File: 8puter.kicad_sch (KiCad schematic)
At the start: 6 parts, among them J1 PWR-DC

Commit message: Serial interface
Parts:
- removed CPU1: W65C816SxP, Package_DIP:DIP-40_W25.4mm_LongPads, symbol 65xx:W65C816SxP
- removed R6: 1K, Resistor_SMD:R_0603_1608Metric, symbol Device:R
- added C2: 1uF, symbol Device:C_Small
- added CPU1: W65C02SxP, Package_DIP:DIP-40_W25.4mm_LongPads, symbol 65xx:W65C02SxP
- added GLUE_FPGA1: (no value), Package_DFN_QFN:QFN-32-1EP_5x5mm_P0.5mm_EP3.1x3.1mm, symbol Custom:﻿MachXO2-256-QFN32
- added JTAG1: (no value), Connector_PinHeader_1.00mm:PinHeader_1x05_P1.00mm_Vertical, symbol Connector_Generic:Conn_01x05
- added R1: 1K, symbol Device:R
- added R3: 4.7K, symbol Device:R
- C3: value 10uF -> 10uF 16V
- C4: footprint Capacitor_SMD:C_1206_3216Metric_Pad1.33x1.80mm_HandSolder -> (none)
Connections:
- net +3V3: now also GLUE_FPGA1.15 (VCCIO2), GLUE_FPGA1.18 (VCC), GLUE_FPGA1.19 (VCCIO1), GLUE_FPGA1.2 (VCC), GLUE_FPGA1.24 (VCCIO0), GLUE_FPGA1.31 (VCCIO0), GLUE_FPGA1.6 (VCCIO3), GLUE_FPGA1.7 (VCCIO2), R1.2
- net +5V: now also C2.1, CPU1.38 (~{SO}), CPU1.8 (VDD)
- net ADDR0: now also CPU1.9 (A0)
- net ADDR1: now also CPU1.10 (A1)
- net ADDR10: now also CPU1.19 (A10)
- net ADDR11: now also CPU1.20 (A11)
- net ADDR12: now also CPU1.22 (A12), GLUE_FPGA1.17 (PB9B/SI)
- net ADDR13: now also CPU1.23 (A13), GLUE_FPGA1.16 (PB9A/SN)
- net ADDR14: now also CPU1.24 (A14), GLUE_FPGA1.14 (PB4D)
- net ADDR15: now also CPU1.25 (A15), GLUE_FPGA1.13 (PB4C)
- net ADDR2: now also CPU1.11 (A2)
- net ADDR3: now also CPU1.12 (A3)
- net ADDR4: now also CPU1.13 (A4)
- net ADDR5: now also CPU1.14 (A5)
- net ADDR6: now also CPU1.15 (A6)
- net ADDR7: now also CPU1.16 (A7)
- net ADDR8: now also CPU1.17 (A8)
- net ADDR9: now also CPU1.18 (A9)
- net BE: now also CPU1.36 (BE), GLUE_FPGA1.10 (PB2D/SPISO)
- net CLOCK: now also CPU1.37 (ϕ0), GLUE_FPGA1.9 (PB2C/SCLK)
- net CPU_R~{W}: now also CPU1.34 (R/~{W}), GLUE_FPGA1.12 (PB4B)
- net GND: now also C2.2, CPU1.21 (VSS), GLUE_FPGA1.22 (GND), GLUE_FPGA1.3 (GND), GLUE_FPGA1.33 (GND), JTAG1.4 (Pin_4), R3.2
- net RDY: now also CPU1.2 (RDY), GLUE_FPGA1.11 (PB4A)
- net ~{IRQ}: now also CPU1.4 (~{IRQ})
- net ~{NMI}: now also CPU1.6 (~{NMI})
- new net: GLUE_FPGA1.26 (PT9A/JTAGENB), R1.1
- new net CPU_W~{R}: GLUE_FPGA1.21 (PR5A)
- new net DATA0: CPU1.33 (D0)
- new net DATA1: CPU1.32 (D1)
- new net DATA2: CPU1.31 (D2)
- new net DATA3: CPU1.30 (D3)
- new net DATA4: CPU1.29 (D4)
- new net DATA5: CPU1.28 (D5)
- new net DATA6: CPU1.27 (D6)
- new net DATA7: CPU1.26 (D7)
- new net TCK: GLUE_FPGA1.30 (PT7A/TCK), JTAG1.2 (Pin_2), R3.1
- new net TDI: GLUE_FPGA1.32 (PT6D/TDI), JTAG1.3 (Pin_3)
- new net TDO: GLUE_FPGA1.1 (PT6C/TDO), JTAG1.5 (Pin_5)
- new net TMS: GLUE_FPGA1.29 (PT7B/TMS), JTAG1.1 (Pin_1)
- new net ~{PRP_CS}: GLUE_FPGA1.25 (PT9B/PROGRAMN)
- new net ~{RAM_CS}: GLUE_FPGA1.28 (PT8C/SCL)
- new net ~{RESET}: CPU1.40 (~{RES})
- new net ~{ROM_CS}: GLUE_FPGA1.27 (PT8D/SDA)
- new net ~{SERIAL_CS}: GLUE_FPGA1.20 (PR5B)
- new net ~{VID_CS}: GLUE_FPGA1.23 (PT9D/DONE)
- no-connect marks 1 -> 8
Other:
- removed sheet Bus Control
- added sheet Serial Controller (sch/serial.kicad_sch)
- sheet Memory Unit ports: added A[0..15], ~{ROM_CS}, ~{SRAM_CS}; removed A[0..23], VA, ~{PRP_CS[0..5]}, ~{VID_CS}
- sheet Peripheral Handler ports: added A[0..15], BUS_R~{W}, ~{PRP_CS}, ~{RESET}; removed BUS_EN, ~{PRP_CS[0..5]}
- sheet Power ports: added ~{RST}; removed RST
- note added: "DEBUG"
- note added: "MEMORY MAP ~{ }"
- note added: "RAM: 0x0000 - 0x7FFF PRP: 0x8000 - 0x8FFF SER: 0x9000 - 0x9FFF VID: 0xA000 - 0xAFFF ROM: 0xB000 - 0xFFFF"
- note added: "This map will be programmed into the FPGA"
- note removed: "Contains ROM, RAM and decode logic."
- note removed: "Debug"
- note removed: "MEMORY"
- company: (none) -> zrthxn
- title: (none) -> 8puter
- moved on the sheet: C3, C4, CRYSTAL0, J1

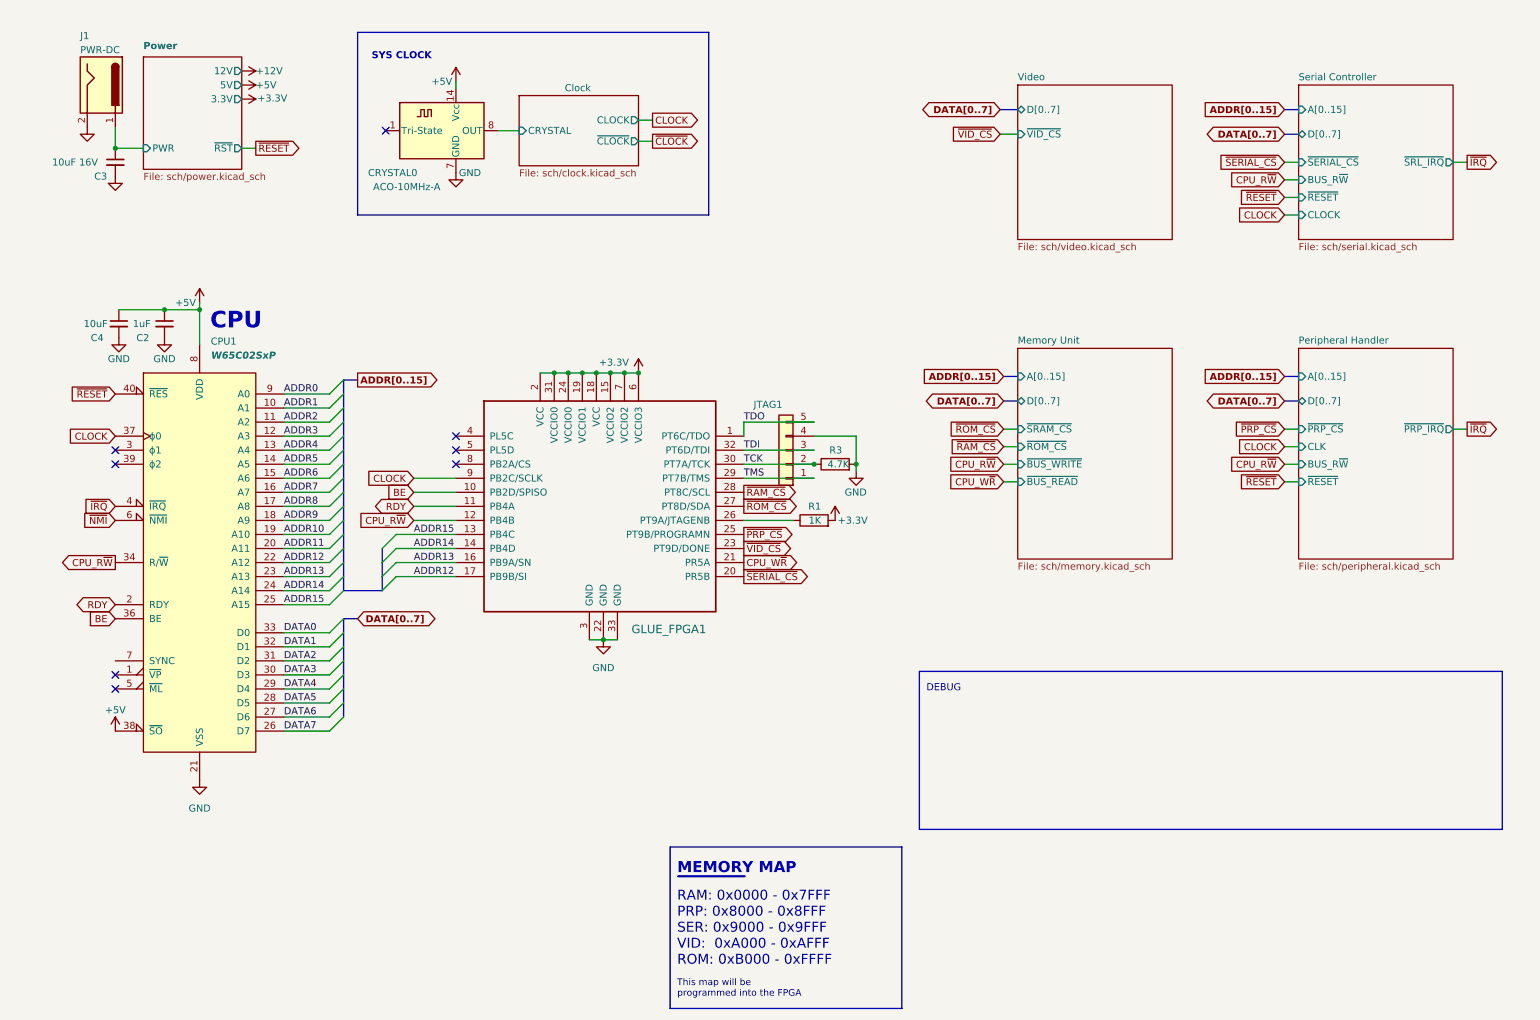
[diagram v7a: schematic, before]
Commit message: Serial, debug and prph headers
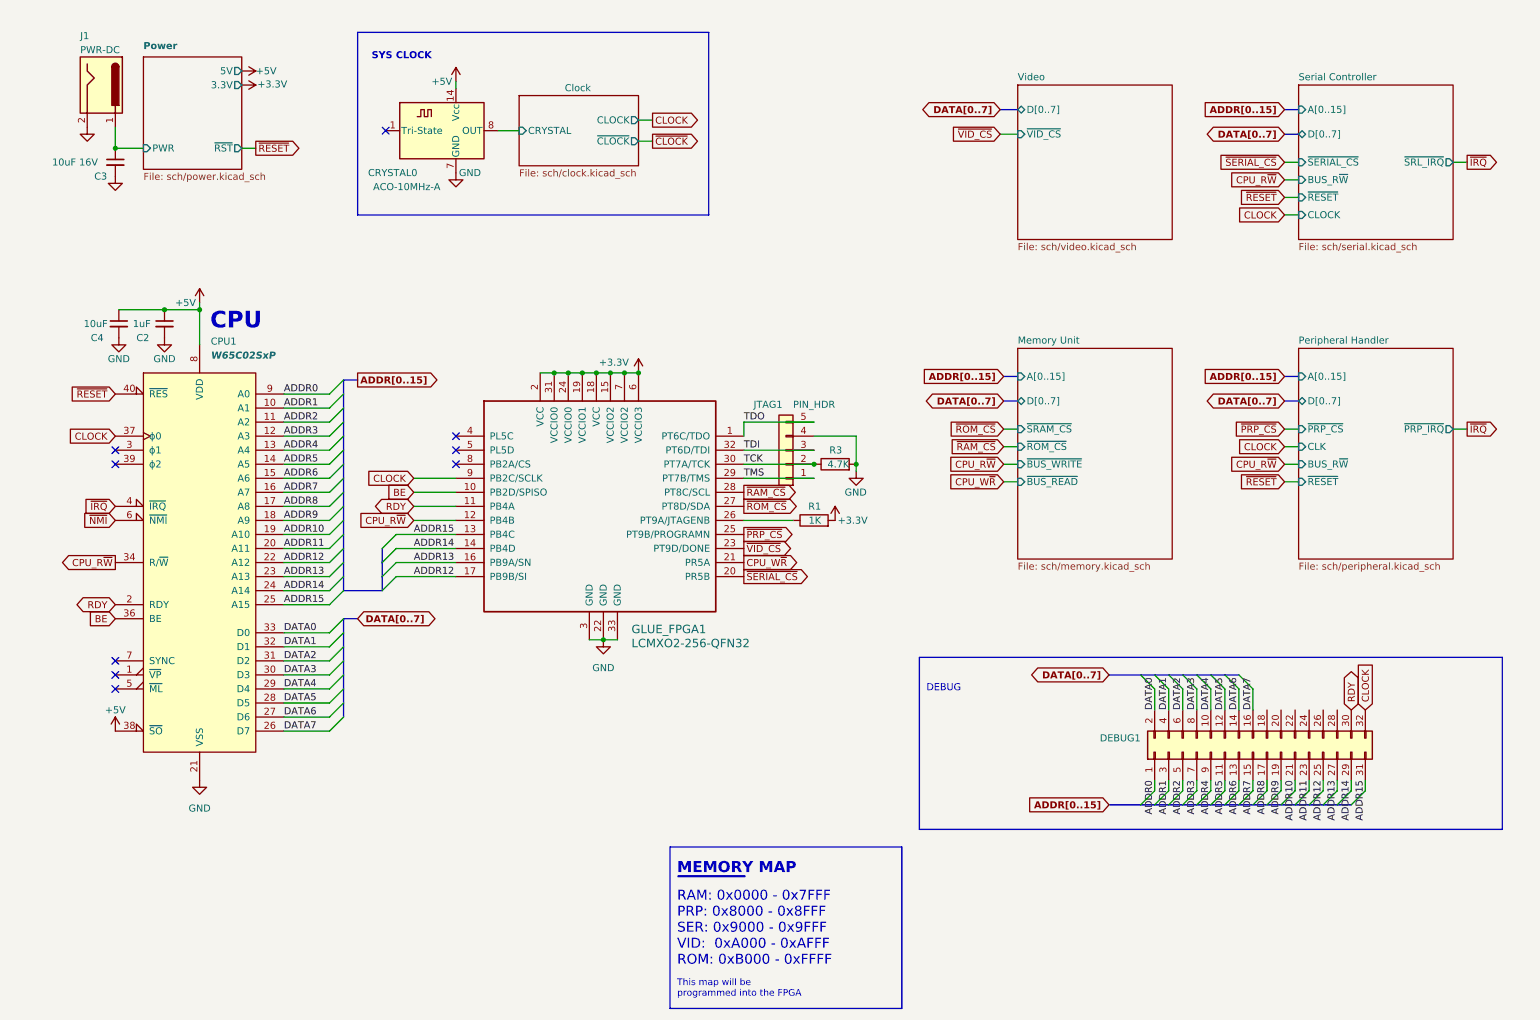
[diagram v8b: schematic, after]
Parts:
- added DEBUG1: (no value), symbol Connector_Generic:Conn_02x16_Odd_Even
- C2, C4: footprint (none) -> Capacitor_SMD:C_0805_2012Metric
- GLUE_FPGA1: value (none) -> LCMXO2-256-QFN32
- JTAG1: value (none) -> PIN_HDR
- R1, R3: footprint (none) -> Resistor_SMD:R_0805_2012Metric
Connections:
- net ADDR0: now also DEBUG1.1 (Pin_1)
- net ADDR1: now also DEBUG1.3 (Pin_3)
- net ADDR10: now also DEBUG1.21 (Pin_21)
- net ADDR11: now also DEBUG1.23 (Pin_23)
- net ADDR12: now also DEBUG1.25 (Pin_25)
- net ADDR13: now also DEBUG1.27 (Pin_27)
- net ADDR14: now also DEBUG1.29 (Pin_29)
- net ADDR15: now also DEBUG1.31 (Pin_31)
- net ADDR2: now also DEBUG1.5 (Pin_5)
- net ADDR3: now also DEBUG1.7 (Pin_7)
- net ADDR4: now also DEBUG1.9 (Pin_9)
- net ADDR5: now also DEBUG1.11 (Pin_11)
- net ADDR6: now also DEBUG1.13 (Pin_13)
- net ADDR7: now also DEBUG1.15 (Pin_15)
- net ADDR8: now also DEBUG1.17 (Pin_17)
- net ADDR9: now also DEBUG1.19 (Pin_19)
- net CLOCK: now also DEBUG1.32 (Pin_32)
- net DATA0: now also DEBUG1.2 (Pin_2)
- net DATA1: now also DEBUG1.4 (Pin_4)
- net DATA2: now also DEBUG1.6 (Pin_6)
- net DATA3: now also DEBUG1.8 (Pin_8)
- net DATA4: now also DEBUG1.10 (Pin_10)
- net DATA5: now also DEBUG1.12 (Pin_12)
- net DATA6: now also DEBUG1.14 (Pin_14)
- net DATA7: now also DEBUG1.16 (Pin_16)
- net RDY: now also DEBUG1.30 (Pin_30)
- no-connect marks 8 -> 9
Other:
- sheet Power ports: added none; removed 12V
